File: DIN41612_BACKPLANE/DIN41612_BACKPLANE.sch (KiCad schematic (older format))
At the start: 28 parts

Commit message: Schematic and PCB done.
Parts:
- removed J? (x6): C64AC, symbol Connector:C64AC
- added H13, H14, H15, H16: MountingHole, MountingHole:MountingHole_3.2mm_M3_DIN965_Pad, symbol Mechanical:MountingHole
- added J10, J11, J12, J13, J8, J9: 5535090-4, DIN41612_Backplane:C96ABC, symbol Connector:C96ABC
- added J14, J5: 71918-150LF, Connector_IDC:IDC-Header_2x25_P2.54mm_Vertical_Lock, symbol Connector_Generic:Conn_02x25_Odd_Even
- D1: renamed from D?; value D_Zener -> MMSZ5249B-E3-18; footprint (none) -> Diode_SMD:D_SOD-123
- D2: renamed from D?; value LED -> RED; footprint (none) -> LED_SMD:LED_0603_1608Metric_Pad1.05x0.95mm_HandSolder
- H1, H10, H11, H12, H2, H3, H4, H5, H6, H7, H8, H9: renamed from H?; footprint (none) -> MountingHole:MountingHole_3.2mm_M3_DIN965_Pad
- J1, J2, J3, J4, J6, J7: renamed from J?; value RJ45_Shielded -> 615008138221; footprint (none) -> DIN41612_Backplane:615008138221
- J15: renamed from J?; value Conn_01x04_Male -> 1829170; footprint (none) -> Connector_Phoenix_GMSTB:PhoenixContact_GMSTBV_2,5_4-GF-7,62_1x04_P7.62mm_Vertical_ThreadedFlange_MountHole
- R1: renamed from R?; value R -> 370; footprint (none) -> Resistor_SMD:R_0603_1608Metric_Pad1.05x0.95mm_HandSolder
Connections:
- net +24V: now also J10.A31 (31A), J10.A32 (32A), J10.B31 (31B), J10.B32 (32B), J10.C31 (31C), J10.C32 (32C), J11.A31 (31A), J11.A32 (32A), J11.B31 (31B), J11.B32 (32B), J11.C31 (31C), J11.C32 (32C), J12.A31 (31A), J12.A32 (32A), J12.B31 (31B), J12.B32 (32B), J12.C31 (31C), J12.C32 (32C), J13.A31 (31A), J13.A32 (32A), J13.B31 (31B), J13.B32 (32B), J13.C31 (31C), J13.C32 (32C), J14.45 (Pin_45), J14.46 (Pin_46), J14.47 (Pin_47), J14.48 (Pin_48), J14.49 (Pin_49), J14.50 (Pin_50), J5.45 (Pin_45), J5.46 (Pin_46), J5.47 (Pin_47), J5.48 (Pin_48), J5.49 (Pin_49), J5.50 (Pin_50), J8.A31 (31A), J8.A32 (32A), J8.B31 (31B), J8.B32 (32B), J8.C31 (31C), J8.C32 (32C), J9.A31 (31A), J9.A32 (32A), J9.B31 (31B), J9.B32 (32B), J9.C31 (31C), J9.C32 (32C)
- net A: now also J10.A2 (2A), J10.B2 (2B), J10.C2 (2C), J11.A2 (2A), J11.B2 (2B), J11.C2 (2C), J12.A2 (2A), J12.B2 (2B), J12.C2 (2C), J13.A2 (2A), J13.B2 (2B), J13.C2 (2C), J14.5 (Pin_5), J14.6 (Pin_6), J5.5 (Pin_5), J5.6 (Pin_6), J8.A2 (2A), J8.B2 (2B), J8.C2 (2C), J9.A2 (2A), J9.B2 (2B), J9.C2 (2C)
- net B: now also J10.A3 (3A), J10.B3 (3B), J10.C3 (3C), J11.A3 (3A), J11.B3 (3B), J11.C3 (3C), J12.A3 (3A), J12.B3 (3B), J12.C3 (3C), J13.A3 (3A), J13.B3 (3B), J13.C3 (3C), J14.7 (Pin_7), J14.8 (Pin_8), J5.7 (Pin_7), J5.8 (Pin_8), J8.A3 (3A), J8.B3 (3B), J8.C3 (3C), J9.A3 (3A), J9.B3 (3B), J9.C3 (3C)
- net C: now also J10.A4 (4A), J10.B4 (4B), J10.C4 (4C), J11.A4 (4A), J11.B4 (4B), J11.C4 (4C), J12.A4 (4A), J12.B4 (4B), J12.C4 (4C), J13.A4 (4A), J13.B4 (4B), J13.C4 (4C), J14.10 (Pin_10), J14.9 (Pin_9), J5.10 (Pin_10), J5.9 (Pin_9), J8.A4 (4A), J8.B4 (4B), J8.C4 (4C), J9.A4 (4A), J9.B4 (4B), J9.C4 (4C)
- net D: now also J10.A5 (5A), J10.B5 (5B), J10.C5 (5C), J11.A5 (5A), J11.B5 (5B), J11.C5 (5C), J12.A5 (5A), J12.B5 (5B), J12.C5 (5C), J13.A5 (5A), J13.B5 (5B), J13.C5 (5C), J14.11 (Pin_11), J14.12 (Pin_12), J5.11 (Pin_11), J5.12 (Pin_12), J8.A5 (5A), J8.B5 (5B), J8.C5 (5C), J9.A5 (5A), J9.B5 (5B), J9.C5 (5C)
- net E: now also J10.A6 (6A), J10.B6 (6B), J10.C6 (6C), J11.A6 (6A), J11.B6 (6B), J11.C6 (6C), J12.A6 (6A), J12.B6 (6B), J12.C6 (6C), J13.A6 (6A), J13.B6 (6B), J13.C6 (6C), J14.13 (Pin_13), J14.14 (Pin_14), J5.13 (Pin_13), J5.14 (Pin_14), J8.A6 (6A), J8.B6 (6B), J8.C6 (6C), J9.A6 (6A), J9.B6 (6B), J9.C6 (6C)
- net F: now also J10.A7 (7A), J10.B7 (7B), J10.C7 (7C), J11.A7 (7A), J11.B7 (7B), J11.C7 (7C), J12.A7 (7A), J12.B7 (7B), J12.C7 (7C), J13.A7 (7A), J13.B7 (7B), J13.C7 (7C), J14.15 (Pin_15), J14.16 (Pin_16), J5.15 (Pin_15), J5.16 (Pin_16), J8.A7 (7A), J8.B7 (7B), J8.C7 (7C), J9.A7 (7A), J9.B7 (7B), J9.C7 (7C)
- net G: now also J10.A8 (8A), J10.B8 (8B), J10.C8 (8C), J11.A8 (8A), J11.B8 (8B), J11.C8 (8C), J12.A8 (8A), J12.B8 (8B), J12.C8 (8C), J13.A8 (8A), J13.B8 (8B), J13.C8 (8C), J14.17 (Pin_17), J14.18 (Pin_18), J5.17 (Pin_17), J5.18 (Pin_18), J8.A8 (8A), J8.B8 (8B), J8.C8 (8C), J9.A8 (8A), J9.B8 (8B), J9.C8 (8C)
- net GND1: now also J8.A18 (18A), J8.A22 (22A), J8.B18 (18B), J8.B22 (22B), J8.C18 (18C), J8.C22 (22C)
- net GND2: now also J9.A18 (18A), J9.A22 (22A), J9.B18 (18B), J9.B22 (22B), J9.C18 (18C), J9.C22 (22C)
- net GND3: now also J10.A18 (18A), J10.A22 (22A), J10.B18 (18B), J10.B22 (22B), J10.C18 (18C), J10.C22 (22C)
- net GND4: now also J11.A18 (18A), J11.A22 (22A), J11.B18 (18B), J11.B22 (22B), J11.C18 (18C), J11.C22 (22C)
- net GND5: now also J12.A18 (18A), J12.A22 (22A), J12.B18 (18B), J12.B22 (22B), J12.C18 (18C), J12.C22 (22C)
- net GND6: now also J13.A18 (18A), J13.A22 (22A), J13.B18 (18B), J13.B22 (22B), J13.C18 (18C), J13.C22 (22C)
- net GNDPWR: now also J10.A27 (27A), J10.A28 (28A), J10.B27 (27B), J10.B28 (28B), J10.C27 (27C), J10.C28 (28C), J11.A27 (27A), J11.A28 (28A), J11.B27 (27B), J11.B28 (28B), J11.C27 (27C), J11.C28 (28C), J12.A27 (27A), J12.A28 (28A), J12.B27 (27B), J12.B28 (28B), J12.C27 (27C), J12.C28 (28C), J13.A27 (27A), J13.A28 (28A), J13.B27 (27B), J13.B28 (28B), J13.C27 (27C), J13.C28 (28C), J14.35 (Pin_35), J14.36 (Pin_36), J14.37 (Pin_37), J14.38 (Pin_38), J14.39 (Pin_39), J14.40 (Pin_40), J5.35 (Pin_35), J5.36 (Pin_36), J5.37 (Pin_37), J5.38 (Pin_38), J5.39 (Pin_39), J5.40 (Pin_40), J8.A27 (27A), J8.A28 (28A), J8.B27 (27B), J8.B28 (28B), J8.C27 (27C), J8.C28 (28C), J9.A27 (27A), J9.A28 (28A), J9.B27 (27B), J9.B28 (28B), J9.C27 (27C), J9.C28 (28C)
- net H: now also J10.A9 (9A), J10.B9 (9B), J10.C9 (9C), J11.A9 (9A), J11.B9 (9B), J11.C9 (9C), J12.A9 (9A), J12.B9 (9B), J12.C9 (9C), J13.A9 (9A), J13.B9 (9B), J13.C9 (9C), J14.19 (Pin_19), J14.20 (Pin_20), J5.19 (Pin_19), J5.20 (Pin_20), J8.A9 (9A), J8.B9 (9B), J8.C9 (9C), J9.A9 (9A), J9.B9 (9B), J9.C9 (9C)
- net I: now also J10.A10 (10A), J10.B10 (10B), J10.C10 (10C), J11.A10 (10A), J11.B10 (10B), J11.C10 (10C), J12.A10 (10A), J12.B10 (10B), J12.C10 (10C), J13.A10 (10A), J13.B10 (10B), J13.C10 (10C), J14.21 (Pin_21), J14.22 (Pin_22), J5.21 (Pin_21), J5.22 (Pin_22), J8.A10 (10A), J8.B10 (10B), J8.C10 (10C), J9.A10 (10A), J9.B10 (10B), J9.C10 (10C)
- net K: now also J10.A11 (11A), J10.B11 (11B), J10.C11 (11C), J11.A11 (11A), J11.B11 (11B), J11.C11 (11C), J12.A11 (11A), J12.B11 (11B), J12.C11 (11C), J13.A11 (11A), J13.B11 (11B), J13.C11 (11C), J14.23 (Pin_23), J14.24 (Pin_24), J5.23 (Pin_23), J5.24 (Pin_24), J8.A11 (11A), J8.B11 (11B), J8.C11 (11C), J9.A11 (11A), J9.B11 (11B), J9.C11 (11C)
- net L: now also J10.A12 (12A), J10.B12 (12B), J10.C12 (12C), J11.A12 (12A), J11.B12 (12B), J11.C12 (12C), J12.A12 (12A), J12.B12 (12B), J12.C12 (12C), J13.A12 (12A), J13.B12 (12B), J13.C12 (12C), J14.25 (Pin_25), J14.26 (Pin_26), J5.25 (Pin_25), J5.26 (Pin_26), J8.A12 (12A), J8.B12 (12B), J8.C12 (12C), J9.A12 (12A), J9.B12 (12B), J9.C12 (12C)
- net M: now also J10.A13 (13A), J10.B13 (13B), J10.C13 (13C), J11.A13 (13A), J11.B13 (13B), J11.C13 (13C), J12.A13 (13A), J12.B13 (13B), J12.C13 (13C), J13.A13 (13A), J13.B13 (13B), J13.C13 (13C), J14.27 (Pin_27), J14.28 (Pin_28), J5.27 (Pin_27), J5.28 (Pin_28), J8.A13 (13A), J8.B13 (13B), J8.C13 (13C), J9.A13 (13A), J9.B13 (13B), J9.C13 (13C)
- net RX1+: now also J8.A20 (20A)
- net RX1-: now also J8.A21 (21A)
- net RX2+: now also J9.A20 (20A)
- net RX2-: now also J9.A21 (21A)
- net RX3+: now also J10.A20 (20A)
- net RX3-: now also J10.A21 (21A)
- net RX4+: now also J11.A20 (20A)
- net RX4-: now also J11.A21 (21A)
- net RX5+: now also J12.A20 (20A)
- net RX5-: now also J12.A21 (21A)
- net RX6+: now also J13.A20 (20A)
- net RX6-: now also J13.A21 (21A)
- net TX1+: now also J8.C20 (20C)
- net TX1-: now also J8.C21 (21C)
- net TX2+: now also J9.C20 (20C)
- net TX2-: now also J9.C21 (21C)
- net TX3+: now also J10.C20 (20C)
- net TX3-: now also J10.C21 (21C)
- net TX4+: now also J11.C20 (20C)
- net TX4-: now also J11.C21 (21C)
- net TX5+: now also J12.C20 (20C)
- net TX5-: now also J12.C21 (21C)
- net TX6+: now also J13.C20 (20C)
- net TX6-: now also J13.C21 (21C)
- no-connect marks 168 -> 280
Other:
- note added: "1806009"
- moved on the sheet: H1, H10, H11, H12, H2, H3, H4, H5, H6, H7, H8, H9

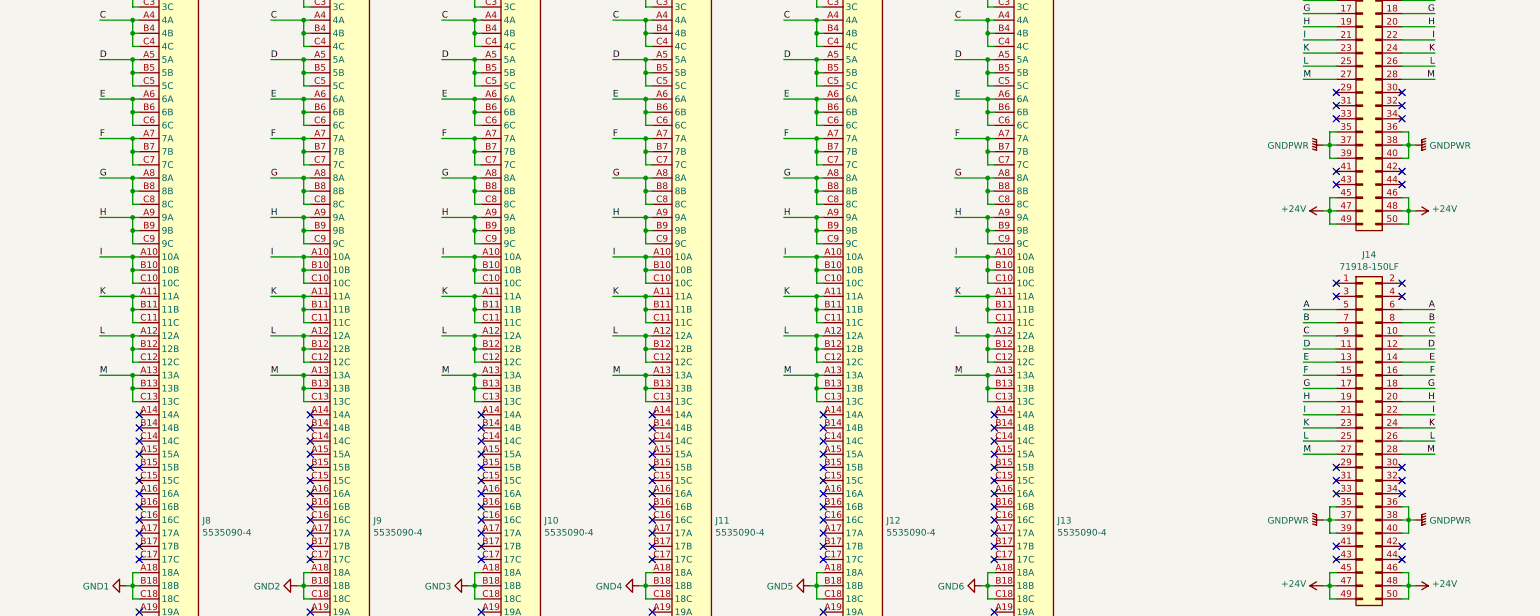
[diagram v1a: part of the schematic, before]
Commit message: Added trigger signal.
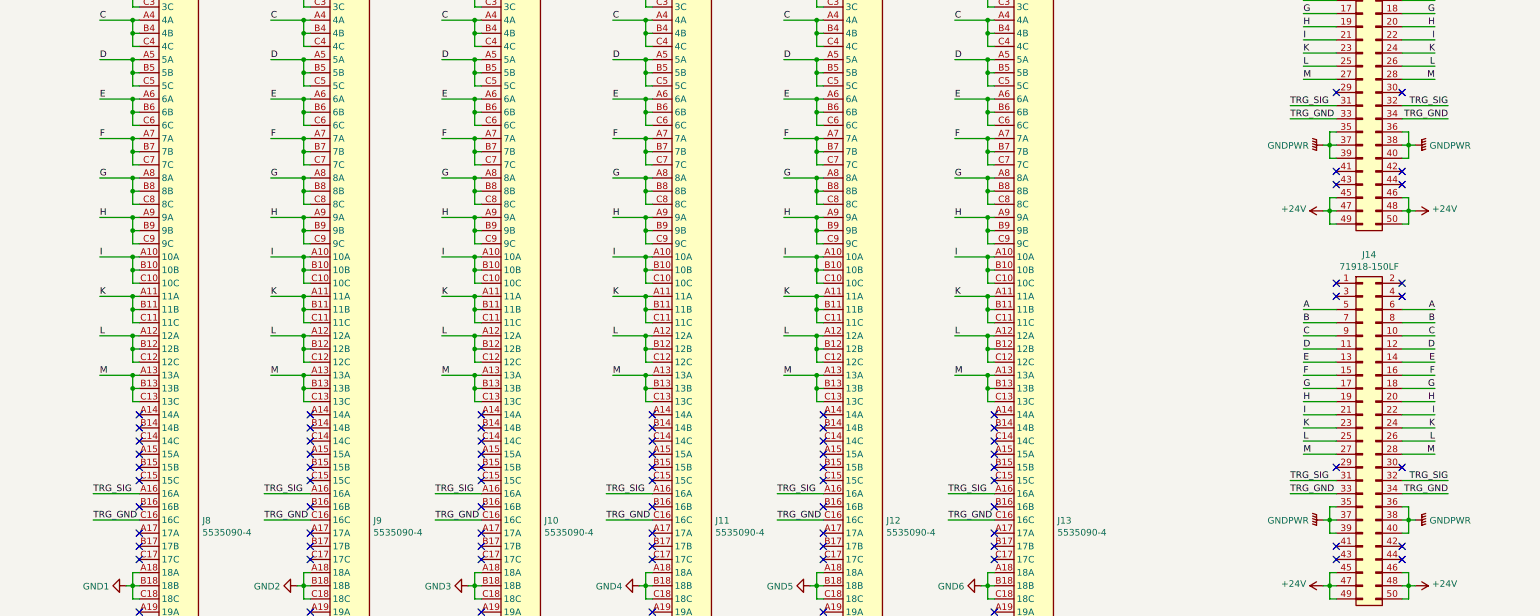
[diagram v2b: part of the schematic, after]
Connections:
- net TRG_SIG: now reaches J8.A16 (16A)
- net TRG_SIG: now also J10.A16 (16A), J11.A16 (16A), J12.A16 (16A), J13.A16 (16A), J14.31 (Pin_31), J14.32 (Pin_32), J5.31 (Pin_31), J5.32 (Pin_32), J9.A16 (16A)
- net TRG_GND: now reaches J8.C16 (16C)
- net TRG_GND: now also J10.C16 (16C), J11.C16 (16C), J12.C16 (16C), J13.C16 (16C), J14.33 (Pin_33), J14.34 (Pin_34), J5.33 (Pin_33), J5.34 (Pin_34), J9.C16 (16C)
- no-connect marks 280 -> 260
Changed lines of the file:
@@
 Wire Wire Line
 	13400 1300 13150 1300
-NoConn ~ 13400 2600
-NoConn ~ 13400 2700
 Text Label 14150 2400 2    50   ~ 0
 M
@@
 Wire Wire Line
 	14000 3400 13950 3400
-NoConn ~ 13900 2600
-NoConn ~ 13900 2700
 NoConn ~ 13900 3100
 NoConn ~ 13900 3200
@@
 NoConn ~ 4300 5350
 NoConn ~ 4300 5450
-NoConn ~ 4300 5550
 NoConn ~ 4300 5650
-NoConn ~ 4300 5750
-NoConn ~ 4300 5850
 NoConn ~ 4300 5950
-NoConn ~ 4300 6050
 Wire Wire Line
 	5600 1350 5550 1350
@@
 NoConn ~ 5600 5350
 NoConn ~ 5600 5450
-NoConn ~ 5600 5550
 NoConn ~ 5600 5650
-NoConn ~ 5600 5750
-NoConn ~ 5600 5850
 NoConn ~ 5600 5950
-NoConn ~ 5600 6050
 $Comp
 L DIN41612_BACKPLANE:GND2 #PWR012
@@
 NoConn ~ 6900 5350
 NoConn ~ 6900 5450
-NoConn ~ 6900 5550
 NoConn ~ 6900 5650
-NoConn ~ 6900 5750
-NoConn ~ 6900 5850
 NoConn ~ 6900 5950
-NoConn ~ 6900 6050
 $Comp
 L DIN41612_BACKPLANE:GND3 #PWR013
@@
 NoConn ~ 8200 5350
 NoConn ~ 8200 5450
-NoConn ~ 8200 5550
 NoConn ~ 8200 5650
-NoConn ~ 8200 5750
-NoConn ~ 8200 5850
 NoConn ~ 8200 5950
-NoConn ~ 8200 6050
 $Comp
 L DIN41612_BACKPLANE:GND4 #PWR022
@@
 NoConn ~ 9500 5350
 NoConn ~ 9500 5450
-NoConn ~ 9500 5550
 NoConn ~ 9500 5650
-NoConn ~ 9500 5750
 NoConn ~ 9500 5850
 NoConn ~ 9500 5950
@@
 NoConn ~ 10800 5350
 NoConn ~ 10800 5450
-NoConn ~ 10800 5550
 NoConn ~ 10800 5650
-NoConn ~ 10800 5750
 NoConn ~ 10800 5850
 NoConn ~ 10800 5950
@@
 Wire Wire Line
 	13400 4150 13150 4150
-NoConn ~ 13400 5450
-NoConn ~ 13400 5550
 Text Label 14150 5250 2    50   ~ 0
 M
@@
 Wire Wire Line
 	14000 6250 13950 6250
-NoConn ~ 13900 5450
-NoConn ~ 13900 5550
 NoConn ~ 13900 5950
 NoConn ~ 13900 6050
@@
 	1    0    0    -1
 $EndComp
+Text Label 13050 5550 0    50   ~ 0
+TRG_GND
+Wire Wire Line
+	13400 5550 13050 5550
+Wire Wire Line
+	13400 5450 13050 5450
+Text Label 13050 5450 0    50   ~ 0
+TRG_SIG
+Text Label 14250 5550 2    50   ~ 0
+TRG_GND
+Wire Wire Line
+	13900 5550 14250 5550
+Wire Wire Line
+	13900 5450 14250 5450
+Text Label 14250 5450 2    50   ~ 0
+TRG_SIG
+Text Label 13050 2700 0    50   ~ 0
+TRG_GND
+Wire Wire Line
+	13400 2700 13050 2700
+Wire Wire Line
+	13400 2600 13050 2600
+Text Label 13050 2600 0    50   ~ 0
+TRG_SIG
+Text Label 14250 2700 2    50   ~ 0
+TRG_GND
+Wire Wire Line
+	13900 2700 14250 2700
+Wire Wire Line
+	13900 2600 14250 2600
+Text Label 14250 2600 2    50   ~ 0
+TRG_SIG
+Text Label 3950 5750 0    50   ~ 0
+TRG_GND
+Wire Wire Line
+	4300 5750 3950 5750
+Wire Wire Line
+	4300 5550 3950 5550
+Text Label 3950 5550 0    50   ~ 0
+TRG_SIG
+Text Label 5250 5750 0    50   ~ 0
+TRG_GND
+Wire Wire Line
+	5600 5750 5250 5750
+Wire Wire Line
+	5600 5550 5250 5550
+Text Label 5250 5550 0    50   ~ 0
+TRG_SIG
+Text Label 7850 5750 0    50   ~ 0
+TRG_GND
+Wire Wire Line
+	8200 5750 7850 5750
+Wire Wire Line
+	8200 5550 7850 5550
+Text Label 7850 5550 0    50   ~ 0
+TRG_SIG
+NoConn ~ 4300 5850
+NoConn ~ 4300 6050
+NoConn ~ 5600 5850
+NoConn ~ 5600 6050
+Text Label 6550 5750 0    50   ~ 0
+TRG_GND
+Wire Wire Line
+	6900 5750 6550 5750
+Wire Wire Line
+	6900 5550 6550 5550
+Text Label 6550 5550 0    50   ~ 0
+TRG_SIG
+NoConn ~ 6900 5850
+NoConn ~ 6900 6050
+NoConn ~ 8200 5850
+NoConn ~ 8200 6050
+Text Label 9150 5750 0    50   ~ 0
+TRG_GND
+Wire Wire Line
+	9500 5750 9150 5750
+Wire Wire Line
+	9500 5550 9150 5550
+Text Label 9150 5550 0    50   ~ 0
+TRG_SIG
+Text Label 10450 5750 0    50   ~ 0
+TRG_GND
+Wire Wire Line
+	10800 5750 10450 5750
+Wire Wire Line
+	10800 5550 10450 5550
+Text Label 10450 5550 0    50   ~ 0
+TRG_SIG
 $EndSCHEMATC
